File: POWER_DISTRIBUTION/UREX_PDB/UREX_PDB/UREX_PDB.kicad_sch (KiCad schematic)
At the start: 20 parts, among them IC1 TCAN1044VDDFR, J1 S2B-PH-SM4-TB_LF__SN_, U6 ESP32-WROOM-32E

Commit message: 040722026
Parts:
- added IC5: TPS22997RYZR, SamacSys_Parts:TPS22997RYZR, symbol SamacSys_Parts:TPS22997RYZR
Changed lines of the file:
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@@
+	)
+	(symbol
+		(lib_id "SamacSys_Parts:TPS22997RYZR")
+		(at 86.36 175.26 0)
+		(unit 1)
+		(body_style 1)
+		(exclude_from_sim no)
+		(in_bom yes)
+		(on_board yes)
+		(in_pos_files yes)
+		(dnp no)
+		(fields_autoplaced yes)
+		(property "Reference" "IC5"
+			(at 102.87 167.64 0)
+			(show_name no)
+			(do_not_autoplace no)
+			(effects
+				(font
+					(size 1.27 1.27)
+				)
+			)
+		)
+		(property "Value" "TPS22997RYZR"
+			(at 102.87 170.18 0)
+			(show_name no)
+			(do_not_autoplace no)
+			(effects
+				(font
+					(size 1.27 1.27)
+				)
+			)
+		)
+		(property "Footprint" "SamacSys_Parts:TPS22997RYZR"
+			(at 115.57 270.18 0)
+			(hide yes)
+			(show_name no)
+			(do_not_autoplace no)
+			(effects
+				(font
+					(size 1.27 1.27)
+				)
+				(justify left top)
+			)
+		)
+		(property "Datasheet" "https://www.ti.com/lit/gpn/tps22997?HQS=ti-null-null-sf-df-pf-sep-wwe&DCM=yes?hkey=EF798316E3902B6ED9A73243A3159BB0"
+			(at 115.57 370.18 0)
+			(hide yes)
+			(show_name no)
+			(do_not_autoplace no)
+			(effects
+				(font
+					(size 1.27 1.27)
+				)
+				(justify left top)
+			)
+		)
+		(property "Description" "TPS22997 5.5-V, 10-A, 4-m On-Resistance Load Switch with Adjustable Rise Time"
+			(at 86.36 175.26 0)
+			(hide yes)
+			(show_name no)
+			(do_not_autoplace no)
+			(effects
+				(font
+					(size 1.27 1.27)
+				)
+			)
+		)
+		(property "Height" "0.8"
+			(at 115.57 570.18 0)
+			(hide yes)
+			(show_name no)
+			(do_not_autoplace no)
+			(effects
+				(font
+					(size 1.27 1.27)
+				)
+				(justify left top)
+			)
+		)
+		(property "Mouser Part Number" "595-TPS22997RYZR"
+			(at 115.57 670.18 0)
+			(hide yes)
+			(show_name no)
+			(do_not_autoplace no)
+			(effects
+				(font
+					(size 1.27 1.27)
+				)
+				(justify left top)
+			)
+		)
+		(property "Mouser Price/Stock" "https://www.mouser.co.uk/ProductDetail/Texas-Instruments/TPS22997RYZR?qs=amGC7iS6iy986RqKkXLlig%3D%3D"
+			(at 115.57 770.18 0)
+			(hide yes)
+			(show_name no)
+			(do_not_autoplace no)
+			(effects
+				(font
+					(size 1.27 1.27)
+				)
+				(justify left top)
+			)
+		)
+		(property "Manufacturer_Name" "Texas Instruments"
+			(at 115.57 870.18 0)
+			(hide yes)
+			(show_name no)
+			(do_not_autoplace no)
+			(effects
+				(font
+					(size 1.27 1.27)
+				)
+				(justify left top)
+			)
+		)
+		(property "Manufacturer_Part_Number" "TPS22997RYZR"
+			(at 115.57 970.18 0)
+			(hide yes)
+			(show_name no)
+			(do_not_autoplace no)
+			(effects
+				(font
+					(size 1.27 1.27)
+				)
+				(justify left top)
+			)
+		)
+		(pin "4"
+		)
+		(pin "6"
+		)
+		(pin "2"
+		)
+		(pin "1"
+		)
+		(pin "3"
+		)
+		(pin "5"
+		)
+		(pin "7"
+		)
+		(pin "9"
+		)
+		(pin "8"
+		)
+		(pin "10"
+		)
+		(instances
+			(project "UREX_PDB"
+				(path "/a38818e8-e869-45a4-b642-866064a1ec6a"
+					(reference "IC5")
+					(unit 1)
+				)
+			)
+		)
 	)
 	(symbol

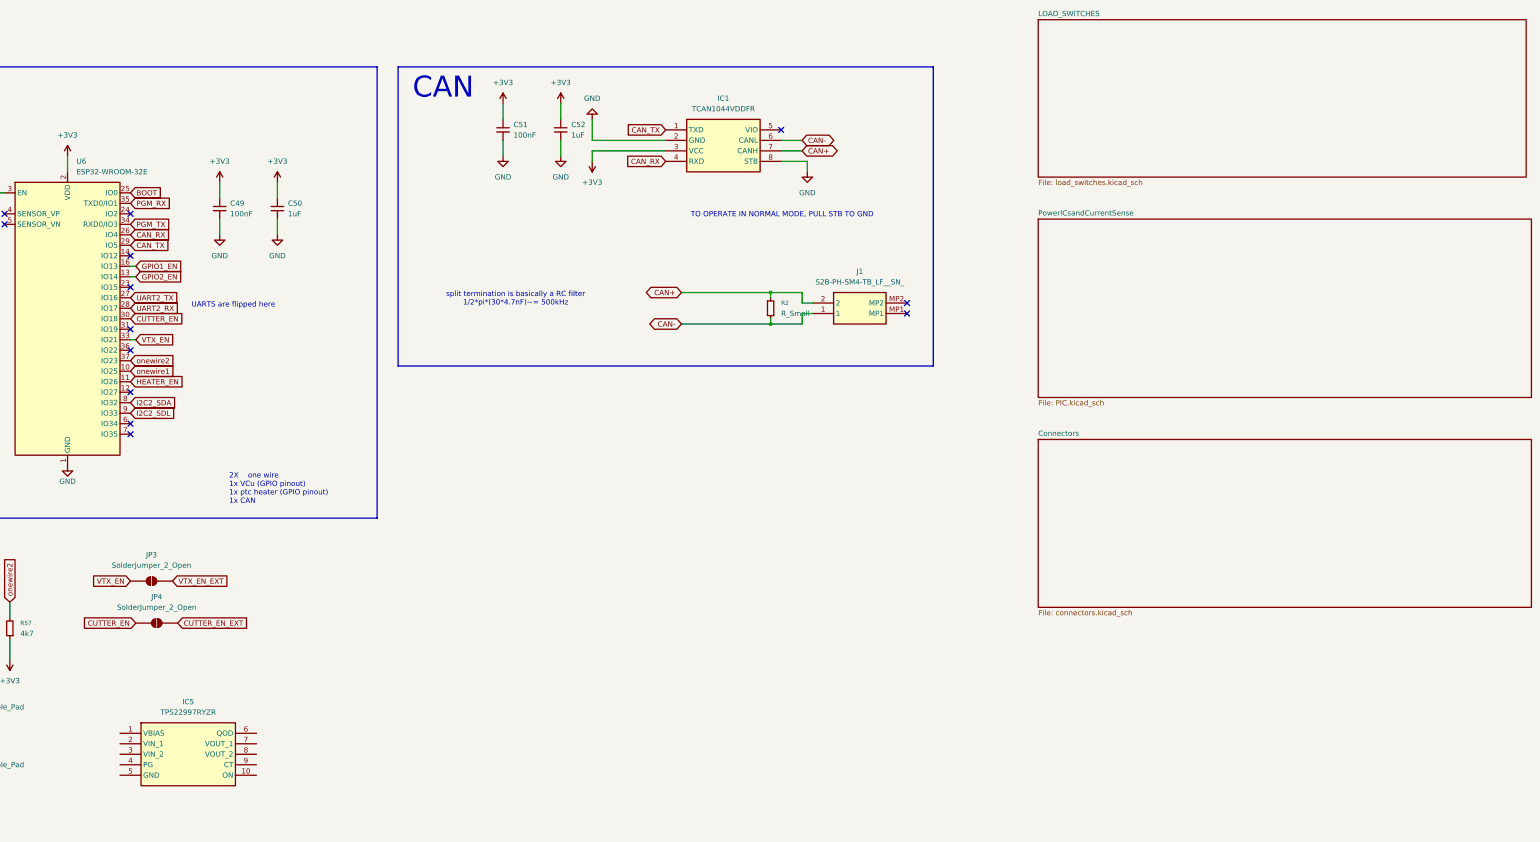
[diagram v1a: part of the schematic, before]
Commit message: Updated to shift register IC
delete VTX_EN or just do some interrupt
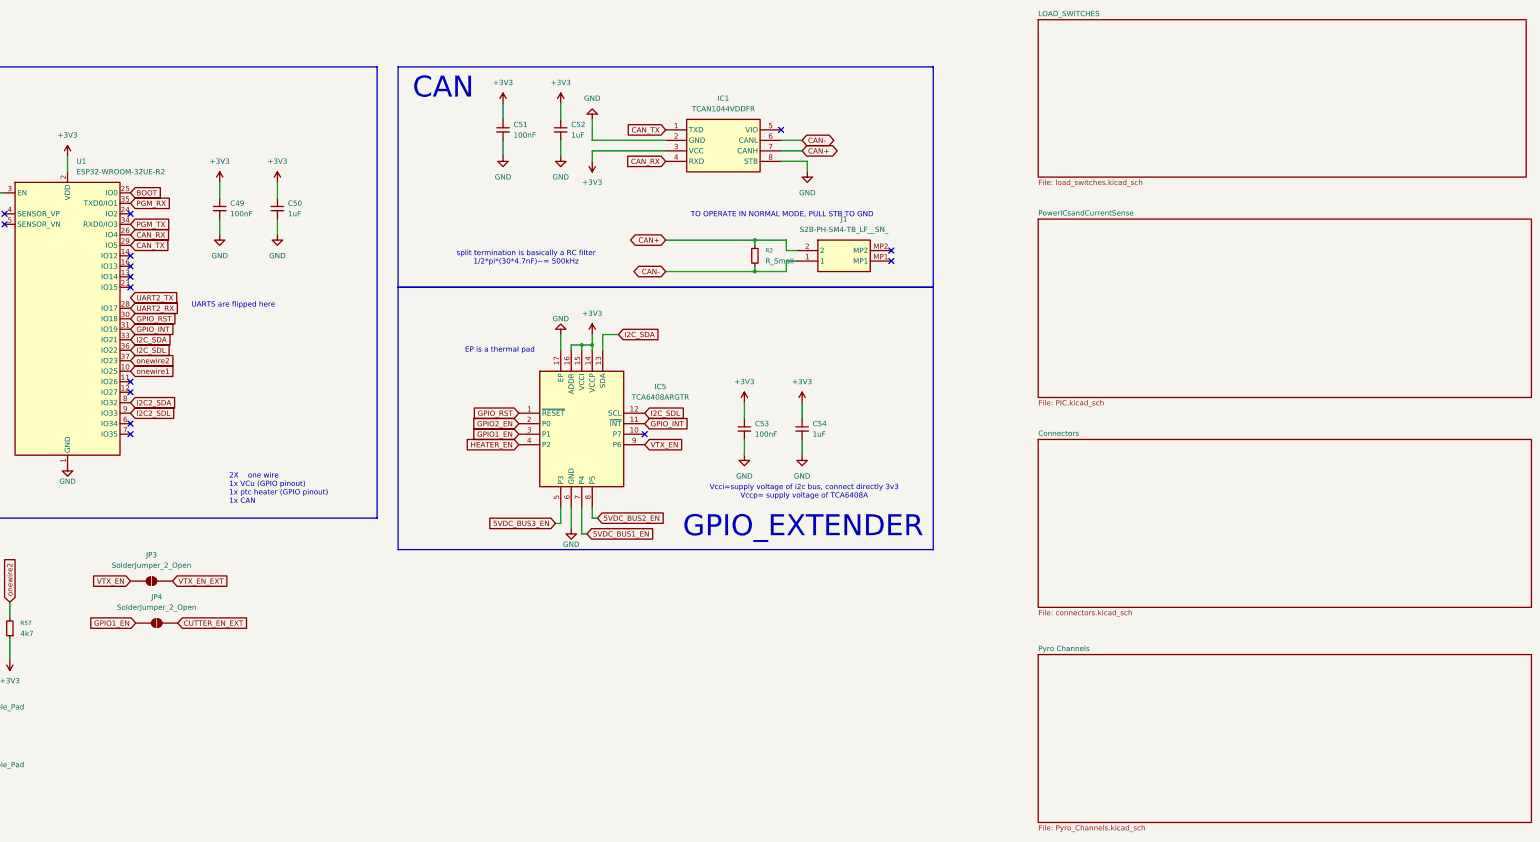
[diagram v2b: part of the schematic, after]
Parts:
- removed IC5: TPS22997RYZR, SamacSys_Parts:TPS22997RYZR, symbol SamacSys_Parts:TPS22997RYZR
- removed U6: ESP32-WROOM-32E, RF_Module:ESP32-WROOM-32D, symbol RF_Module:ESP32-WROOM-32E
- added C53: 100nF, Capacitor_SMD:C_0603_1608Metric, symbol Device:C_Small
- added C54: 1uF, Capacitor_SMD:C_0603_1608Metric, symbol Device:C_Small
- added IC5: TCA6408ARGTR, SamacSys_Parts:QFN50P300X300X100-17N-D, symbol SamacSys_Parts:TCA6408ARGTR
- added U1: ESP32-WROOM-32UE-R2, RF_Module:ESP32-WROOM-32UE, symbol RF_Module:ESP32-WROOM-32UE-R2
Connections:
- net CUTTER_EN is gone; now on net GPIO1_EN: JP4.1 (A)
- net +3V3: now also C53.1, C54.1, IC5.14 (VCCP), IC5.15 (VCCI), IC5.16 (ADDR), U1.2 (VDD), U1.3 (EN)
- net BOOT: now also U1.25 (IO0)
- net CAN_RX: now also U1.26 (IO4)
- net CAN_TX: now also U1.29 (IO5)
- net GND: now also C53.2, C54.2, IC5.17 (EP), IC5.6 (GND), U1.1 (GND), U1.15 (GND), U1.38 (GND), U1.39 (GND)
- net GPIO1_EN: now also IC5.3 (P1)
- net GPIO2_EN: now also IC5.2 (P0)
- net HEATER_EN: now also IC5.4 (P2)
- net I2C2_SDA: now also U1.8 (IO32)
- net I2C2_SDL: now also U1.9 (IO33)
- net PGM_RX: now also U1.35 (TXD0/IO1)
- net PGM_TX: now also U1.34 (RXD0/IO3)
- net UART2_RX: now also U1.28 (IO17)
- net VTX_EN: now also IC5.9 (P6)
- net onewire1: now also U1.10 (IO25)
- net onewire2: now also U1.37 (IO23)
- new net 5VDC_BUS1_EN: IC5.7 (P4)
- new net 5VDC_BUS2_EN: IC5.8 (P5)
- new net 5VDC_BUS3_EN: IC5.5 (P3)
- new net GPIO_INT: IC5.11 (~{INT}), U1.31 (IO19)
- new net GPIO_RST: IC5.1 (~{RESET}), U1.30 (IO18)
- new net I2C_SDA: IC5.13 (SDA), U1.33 (IO21)
- new net I2C_SDL: IC5.12 (SCL), U1.36 (IO22)
- no-connect marks 17 -> 19
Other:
- added sheet Pyro Channels (Pyro_Channels.kicad_sch)
- note added: "EP is a thermal pad"
- note added: "GPIO_EXTENDER"
- note added: "Vcci=supply voltage of i2c bus, connect directly 3v3 Vccp= supply voltage of TCA6408A"
- moved on the sheet: J1, R2

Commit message: production uipdate
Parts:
- R2: value R_Small -> 120r
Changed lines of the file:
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@@
 			)
 		)
-		(property "Value" "R_Small"
+		(property "Value" "120r"
 			(at 242.57 60.9599 0)
 			(show_name no)

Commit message: added 5v 8A  dcdc
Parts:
- C48, C49, C51, C53: value 100nF -> 100nF @50V
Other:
- added sheet HighCurrentDCDC (HighCurrentDCDC.kicad_sch)
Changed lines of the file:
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@@
 			)
 		)
-		(property "Value" "100nF"
+		(property "Value" "100nF @50V"
 			(at 41.91 48.2538 0)
 			(show_name no)
@@
 			)
 		)
-		(property "Value" "100nF"
+		(property "Value" "100nF @50V"
 			(at 113.03 49.5362 0)
 			(show_name no)
@@
 			)
 		)
-		(property "Value" "100nF"
+		(property "Value" "100nF @50V"
 			(at 181.61 30.4862 0)
 			(show_name no)
@@
 			)
 		)
-		(property "Value" "100nF"
+		(property "Value" "100nF @50V"
 			(at 240.03 102.8762 0)
 			(show_name no)
@@
 				)
 			)
+		)
+	)
+	(sheet
+		(at 308.61 -30.48)
+		(size 123.19 25.4)
+		(exclude_from_sim no)
+		(in_bom yes)
+		(on_board yes)
+		(dnp no)
+		(fields_autoplaced yes)
+		(stroke
+			(width 0.1524)
+			(type solid)
+		)
+		(fill
+			(color 0 0 0 0)
+		)
+		(property "Sheetname" "HighCurrentDCDC"
+			(at 308.61 -31.1916 0)
+			(show_name no)
+			(do_not_autoplace no)
+			(effects
+				(font
+					(size 1.27 1.27)
+				)
+				(justify left bottom)
+			)
+		)
+		(property "Sheetfile" "HighCurrentDCDC.kicad_sch"
+			(at 308.61 -4.4954 0)
+			(show_name no)
+			(do_not_autoplace no)
+			(effects
+				(font
+					(size 1.27 1.27)
+				)
+				(justify left top)
+			)
+		)
+		(instances
+			(project "UREX_PDB"
+				(path "/a38818e8-e869-45a4-b642-866064a1ec6a"
+					(page "6")
+				)
+			)

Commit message: V1 Full Fabrication(Freezed design)
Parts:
- removed J1: S2B-PH-SM4-TB_LF__SN_, SamacSys_Parts:S2BPHSM4TBLFSN, symbol SamacSys_Parts:S2B-PH-SM4-TB_LF__SN_
- added J12: S3B-PH-SM4-TB_LF__SN_, SamacSys_Parts:S3BPHSM4TBLFSN, symbol SamacSys_Parts:S3B-PH-SM4-TB_LF__SN_
- H5, H7, H8: footprint MountingHole:MountingHole_2.2mm_M2_ISO7380_Pad -> MountingHole:MountingHole_2.2mm_M2_ISO7380; now in the parts list
- H6: footprint MountingHole:MountingHole_2.2mm_M2_ISO7380_Pad -> MountingHole:MountingHole_2.2mm_M2_Pad_Via; now in the parts list
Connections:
- net CAN+: now also J12.3
- net CAN-: now also J12.2
- net GND: now also H5.1, J12.1
- no-connect marks 19 -> 18
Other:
- moved on the sheet: R2

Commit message: Production push(Version 1)
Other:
- note added: "reset is active low!"
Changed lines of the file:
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@@
+		)
+	)
+	(text "reset is active low!\n"
+		(exclude_from_sim no)
+		(at 248.412 82.042 0)
+		(effects
+			(font
+				(size 1.27 1.27)
+			)
 		)
 	)
